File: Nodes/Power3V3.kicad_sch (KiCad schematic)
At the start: 15 parts, among them U3 LT3970EMS#TRPBF

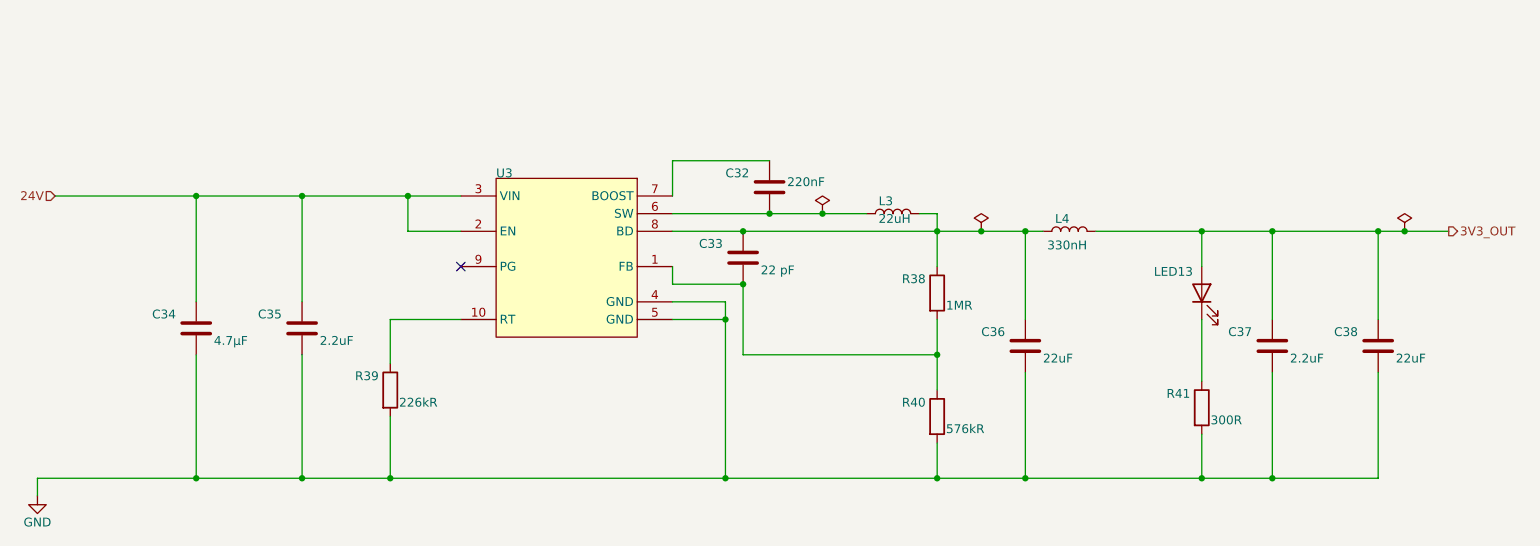
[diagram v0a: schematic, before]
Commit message: Nodes v2.1.2 Improved
- Improved schematic design
- Added two 4.7 uF caps according to the datasheets of the microchips
- Other small changes
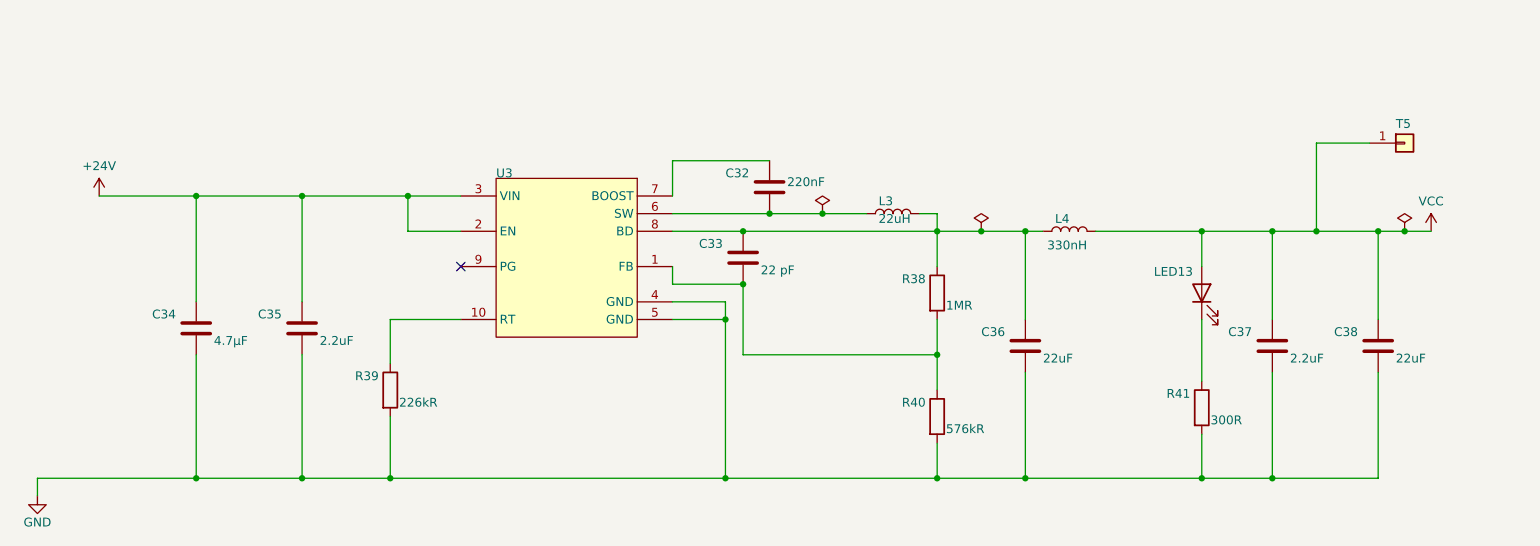
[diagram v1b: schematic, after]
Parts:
- added T5: Conn_01x01, TestPoint:TestPoint_THTPad_D1.5mm_Drill0.7mm, symbol Connector_Generic:Conn_01x01
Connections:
- net 24V renamed +24V
- net 3V3_OUT renamed VCC
- net VCC: now also T5.1 (Pin_1)

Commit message: Nodes v2.2
- This version not compatible with BOB v.2.1.2 and older!
- Completely new layout design
- New power supply system with new voltage regulators
- New microchip STM32G431RBTx for the Analog Node
- New connection system (instead of 18 pin headers now 8 pin and pins were grouped by functions)
- Reduced size of the board by 5%
- Removed power switch for the Analog Node (because this functionality is now provided by a separate voltage regulator. for a more stable voltage)
- Removable ground from the holes added
- Layer numbers added
- Small improvements of the components information were made
- New oscillator for the Nodes
- Removed CAN1, so now only one CAN connection due to the capabilities of the new microchip
- Other small changes and fixes on the schematic and design
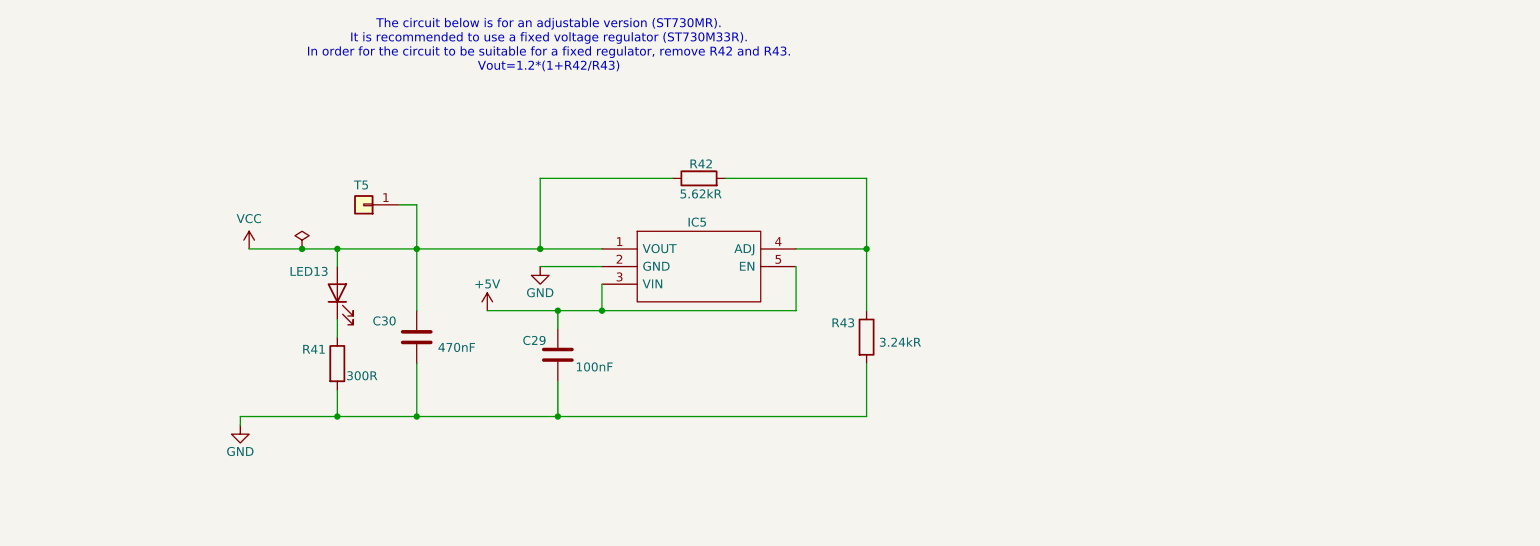
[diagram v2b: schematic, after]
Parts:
- removed C32: 220nF, Capacitor_SMD:C_0805_2012Metric_Pad1.18x1.45mm_HandSolder, symbol Device:C
- removed C33: 22 pF, Capacitor_SMD:C_0805_2012Metric_Pad1.18x1.45mm_HandSolder, symbol Device:C
- removed C34: 4.7µF, Capacitor_SMD:C_0805_2012Metric_Pad1.18x1.45mm_HandSolder, symbol Device:C
- removed C35, C37: 2.2uF, Capacitor_SMD:C_0805_2012Metric_Pad1.18x1.45mm_HandSolder, symbol Device:C
- removed C36, C38: 22 uF, Capacitor_SMD:C_0805_2012Metric_Pad1.18x1.45mm_HandSolder, symbol Device:C
- removed L3: 22uH, Inductor_SMD:L_0805_2012Metric_Pad1.15x1.40mm_HandSolder, symbol Device:L
- removed L4: 330nH, Inductor_SMD:L_0805_2012Metric_Pad1.15x1.40mm_HandSolder, symbol Device:L
- removed R38: 1MR, Resistor_SMD:R_0805_2012Metric_Pad1.20x1.40mm_HandSolder, symbol Device:R
- removed R39: 226kR, Resistor_SMD:R_0805_2012Metric_Pad1.20x1.40mm_HandSolder, symbol Device:R
- removed R40: 576kR, Resistor_SMD:R_0805_2012Metric_Pad1.20x1.40mm_HandSolder, symbol Device:R
- removed U3: LT3970EMS#TRPBF, Vault:LT-MS-10_N, symbol Untitled-altium-import:root_0_LT-LT3970_B-MS-10
- added C29: 100nF, Capacitor_SMD:C_0805_2012Metric_Pad1.18x1.45mm_HandSolder, symbol Device:C
- added C30: 470nF, Capacitor_SMD:C_0805_2012Metric_Pad1.18x1.45mm_HandSolder, symbol Device:C
- added IC5: ST730MR, Regulators:SOT95P280X145-5N, symbol Regulator_Linear:ST730MR
- added R42: 5.62kR, Resistor_SMD:R_0805_2012Metric_Pad1.20x1.40mm_HandSolder, symbol Device:R
- added R43: 3.24kR, Resistor_SMD:R_0805_2012Metric_Pad1.20x1.40mm_HandSolder, symbol Device:R
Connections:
- net GND: now also C29.2, C30.2, IC5.2 (GND), R43.2
- net VCC: now also C30.1, IC5.1 (VOUT), R42.1
- new net: IC5.4 (ADJ), R42.2, R43.1
- new net +5V: C29.1, IC5.3 (VIN), IC5.5 (EN)
- no-connect marks 1 -> 0
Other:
- note added: "The circuit below is for an adjustable version (ST730MR). It is recommended to use a fixed voltage regulator (ST730M33R). In order for the circuit to be suitable for a fixed regulator, remove R42 and R43. Vout=1.2*(1+R42/R43)"

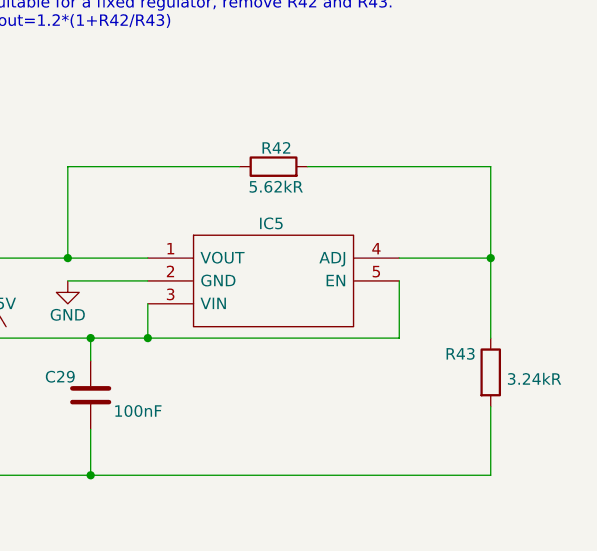
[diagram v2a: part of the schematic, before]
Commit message: Nodes v2.2.3
- Added one more PWM Level shifter
- Controllable amplitude of PWM by switches
- Added labels
- Added resistors to solve BOOT issue
- I2C1 pins changed
- More GND vias
- Higher resistance for adjustable voltage regulators
- Other small changes
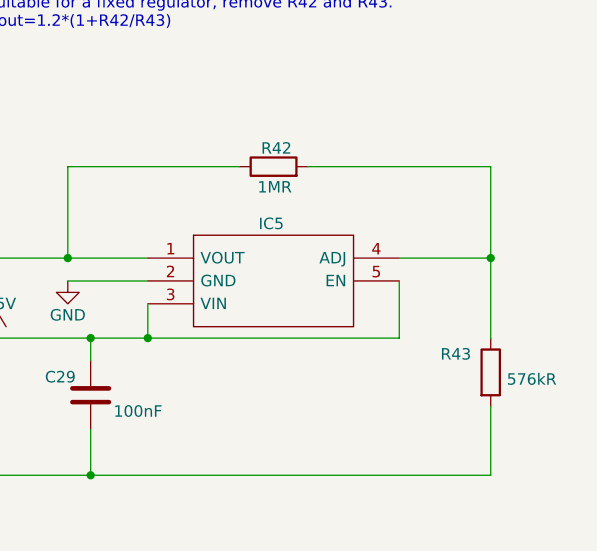
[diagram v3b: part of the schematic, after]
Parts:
- R42: value 5.62kR -> 1MR
- R43: value 3.24kR -> 576kR
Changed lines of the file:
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@@
 		(dnp no)
 		(property "Reference" "R43"
-			(at 172.72 96.52 0)
-			(effects
-				(font
-					(size 1.27 1.27)
-				)
-				(justify left bottom)
-			)
-		)
-		(property "Value" "3.24kR"
+			(at 172.212 96.52 0)
+			(effects
+				(font
+					(size 1.27 1.27)
+				)
+				(justify left bottom)
+			)
+		)
+		(property "Value" "576kR"
 			(at 179.578 99.314 0)
 			(effects
@@
 			)
 		)
-		(property "Description" "ERJ-PB6B3241V"
+		(property "Description" "ERJ-6ENF5763V"
 			(at 177.8 97.79 0)
 			(effects
@@
 			)
 		)
-		(property "Value" "5.62kR"
-			(at 156.972 77.216 90)
+		(property "Value" "1MR"
+			(at 155.702 77.216 90)
 			(effects
 				(font
@@
 			)
 		)
-		(property "Datasheet" "https://www.mouser.fi/datasheet/2/54/cr-1858361.pdf"
+		(property "Datasheet" ""
 			(at 153.67 74.93 0)
 			(effects
@@
 			)
 		)
-		(property "Description" "CR0805-FX-5621ELF"
+		(property "Description" "TNPW08051M00BEEN"
 			(at 153.67 74.93 0)
 			(effects
